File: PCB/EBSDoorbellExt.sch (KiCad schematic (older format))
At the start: 42 parts, among them P1 AC in, P2 Doorbell, Q1 BC846C, SW1 Power, SW2 Test, U1 LM7812CT, U2 LM555N

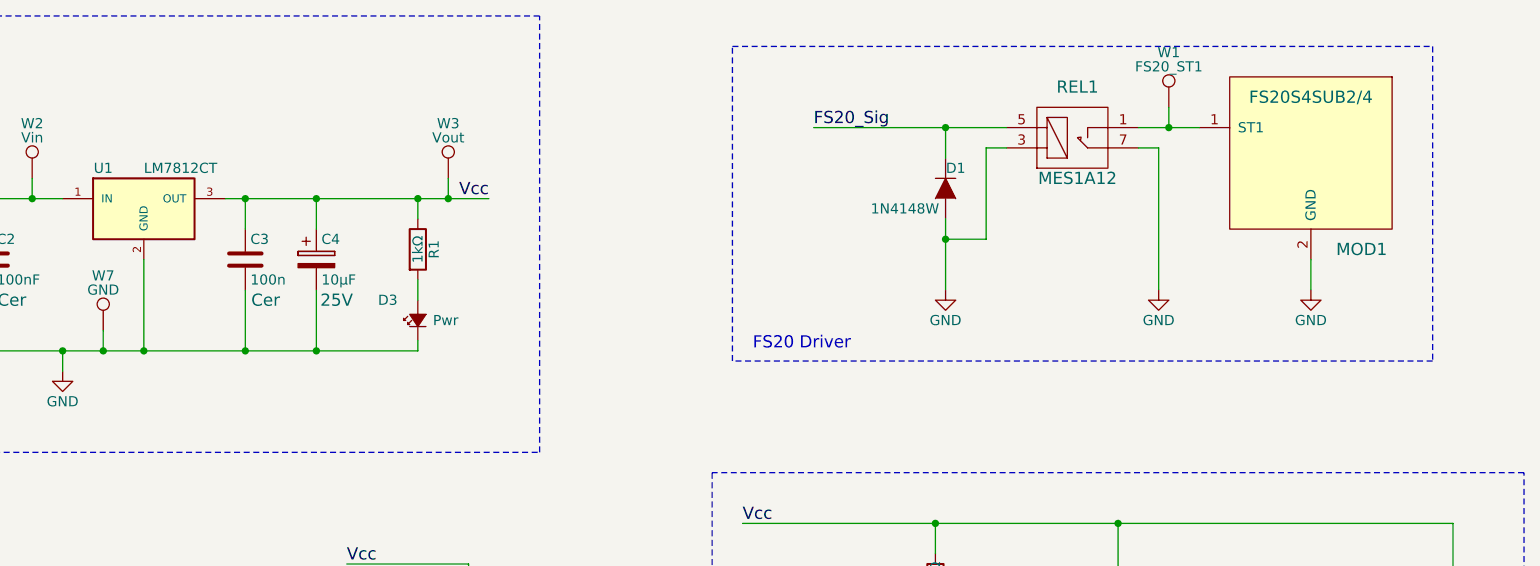
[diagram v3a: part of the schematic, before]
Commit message: Changed the layout to use an Optocoupler instead of a relay and generated Gerbers
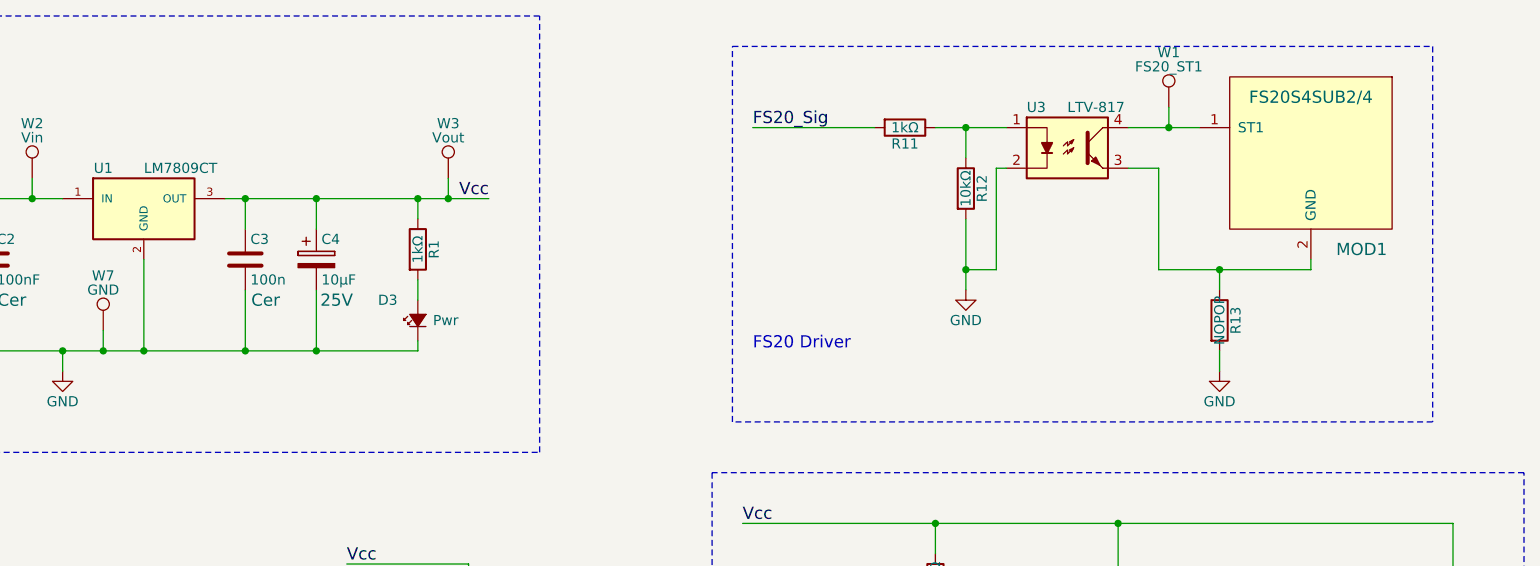
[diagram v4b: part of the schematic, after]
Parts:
- removed D1: 1N4148W, Diodes_SMD:SOD-523, symbol D
- removed REL1: MES1A12, EBSDoorbellExt-Footprints:MES1A12, symbol MES1A12
- added R11: 1kΩ, Resistors_SMD:R_0805_HandSoldering, symbol R
- added R12: 10kΩ, Resistors_SMD:R_0805_HandSoldering, symbol R
- added R13: NOPOP, Resistors_SMD:R_0805_HandSoldering, symbol R
- added U3: LTV-817, EBSDoorbellExt-Footprints:LTV_817, symbol LTV-817
- U1: value LM7812CT -> LM7809CT; footprint TO_SOT_Packages_THT:TO-220_Neutral123_Vertical -> TO_SOT_Packages_THT:TO-220_Neutral123_Horizontal; DigiKeyPN LM7812CTFS-ND -> LM7809ACT-ND
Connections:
- net FS20_Sig: now also R11.2
- net GND: now also R12.2, R13.2, U3.2; no longer MOD1.2 (GND)
- net at MOD1.1 (ST1), W1.1: now also U3.4
- new net: MOD1.2 (GND), R13.1, U3.3
- new net: R11.1, R12.1, U3.1
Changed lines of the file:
@@
 P 3750 1650
 F 0 "U1" H 3550 1850 50  0000 C CNN
-F 1 "LM7812CT" H 3750 1850 50  0000 L CNN
-F 2 "TO_SOT_Packages_THT:TO-220_Neutral123_Vertical" H 3750 1750 50  0001 C CIN
-F 3 "http://www.fairchildsemi.com/datasheets/LM/LM7805.pdf" H 3750 1650 50  0001 C CNN
-F 4 "LM7812CTFS-ND " H 3750 1650 60  0001 C CNN "DigiKeyPN"
+F 1 "LM7809CT" H 3750 1850 50  0000 L CNN
+F 2 "TO_SOT_Packages_THT:TO-220_Neutral123_Horizontal" H 3750 1750 50  0001 C CIN
+F 3 "https://www.fairchildsemi.com/datasheets/LM/LM7805.pdf" H 3750 1650 50  0001 C CNN
+F 4 "LM7809ACT-ND" H 3750 1650 60  0001 C CNN "DigiKeyPN"
 F 5 "Value" H 3750 1650 60  0001 C CNN "Voltage"
 F 6 "Value" H 3750 1650 60  0001 C CNN "ConradPN"
@@
 	5100 2350 5100 2300
 Connection ~ 4600 2350
-$Comp
-L MES1A12 REL1
-U 1 1 57543C1C
-P 8350 1300
-F 0 "REL1" H 8350 1050 60  0000 C CNN
-F 1 "MES1A12" H 8350 1500 60  0000 C CNN
-F 2 "EBSDoorbellExt-Footprints:MES1A12" H 8350 1300 60  0001 C CNN
-F 3 "" H 8350 1300 60  0000 C CNN
-F 4 "Value" H 8350 1300 60  0001 C CNN "DigiKeyPN"
-F 5 "Value" H 8350 1300 60  0001 C CNN "Voltage"
-F 6 "Value" H 8350 1300 60  0001 C CNN "ConradPN"
-F 7 "Value" H 8350 1300 60  0001 C CNN "Link"
-	1    8350 1300
-	1    0    0    1
-$EndComp
-Text Label 7050 1250 0    60   ~ 0
+Text Label 6750 1250 0    60   ~ 0
 FS20_Sig
 $Comp
 L GND #PWR05
 U 1 1 57543E6A
-P 7700 2050
-F 0 "#PWR05" H 7700 1800 50  0001 C CNN
-F 1 "GND" H 7700 1900 50  0000 C CNN
-F 2 "" H 7700 2050 50  0000 C CNN
-F 3 "" H 7700 2050 50  0000 C CNN
-	1    7700 2050
-	1    0    0    -1
-$EndComp
-Wire Wire Line
-	7050 1250 8000 1250
-Wire Wire Line
-	7700 1400 7700 1250
-Connection ~ 7700 1250
-Wire Wire Line
-	7700 1700 7700 2050
-Wire Wire Line
-	7700 1800 7900 1800
-Wire Wire Line
-	7900 1800 7900 1350
-Wire Wire Line
-	7900 1350 8000 1350
-Connection ~ 7700 1800
+P 7800 2050
+F 0 "#PWR05" H 7800 1800 50  0001 C CNN
+F 1 "GND" H 7800 1900 50  0000 C CNN
+F 2 "" H 7800 2050 50  0000 C CNN
+F 3 "" H 7800 2050 50  0000 C CNN
+	1    7800 2050
+	1    0    0    -1
+$EndComp
+Wire Wire Line
+	7650 1250 8000 1250
 $Comp
 L FS20S4SUB2/4-RESCUE-EBSDoorbellExt MOD1
@@
 $EndComp
 Wire Wire Line
-	8950 1250 8650 1250
-Wire Wire Line
-	8650 1350 8750 1350
-Wire Wire Line
-	8750 1350 8750 2050
-$Comp
-L GND #PWR06
-U 1 1 5754503D
-P 8750 2050
-F 0 "#PWR06" H 8750 1800 50  0001 C CNN
-F 1 "GND" H 8750 1900 50  0000 C CNN
-F 2 "" H 8750 2050 50  0000 C CNN
-F 3 "" H 8750 2050 50  0000 C CNN
-	1    8750 2050
-	1    0    0    -1
-$EndComp
-Wire Wire Line
-	9500 1900 9500 2050
-$Comp
-L GND #PWR07
-U 1 1 575450F0
-P 9500 2050
-F 0 "#PWR07" H 9500 1800 50  0001 C CNN
-F 1 "GND" H 9500 1900 50  0000 C CNN
-F 2 "" H 9500 2050 50  0000 C CNN
-F 3 "" H 9500 2050 50  0000 C CNN
-	1    9500 2050
-	1    0    0    -1
-$EndComp
+	8600 1250 8950 1250
 Wire Wire Line
 	2150 2200 2150 2000
@@
 Connection ~ 3550 4250
 $Comp
-L GND #PWR08
+L GND #PWR06
 U 1 1 57548DD0
 P 2450 5200
-F 0 "#PWR08" H 2450 4950 50  0001 C CNN
+F 0 "#PWR06" H 2450 4950 50  0001 C CNN
 F 1 "GND" H 2450 5050 50  0000 C CNN
 F 2 "" H 2450 5200 50  0000 C CNN
@@
 	2450 5200 2450 5050
 $Comp
-L GND #PWR09
+L GND #PWR07
 U 1 1 57548ECC
 P 3250 5200
-F 0 "#PWR09" H 3250 4950 50  0001 C CNN
+F 0 "#PWR07" H 3250 4950 50  0001 C CNN
 F 1 "GND" H 3250 5050 50  0000 C CNN
 F 2 "" H 3250 5200 50  0000 C CNN
@@
 	3250 5200 3250 4900
 $Comp
-L GND #PWR010
+L GND #PWR08
 U 1 1 5754905C
 P 3550 5200
-F 0 "#PWR010" H 3550 4950 50  0001 C CNN
+F 0 "#PWR08" H 3550 4950 50  0001 C CNN
 F 1 "GND" H 3550 5050 50  0000 C CNN
 F 2 "" H 3550 5200 50  0000 C CNN
@@
 Connection ~ 4850 4250
 $Comp
-L GND #PWR011
+L GND #PWR09
 U 1 1 5754947D
 P 4550 5200
-F 0 "#PWR011" H 4550 4950 50  0001 C CNN
+F 0 "#PWR09" H 4550 4950 50  0001 C CNN
 F 1 "GND" H 4550 5050 50  0000 C CNN
 F 2 "" H 4550 5200 50  0000 C CNN
@@
 $EndComp
 $Comp
-L GND #PWR012
+L GND #PWR010
 U 1 1 57549484
 P 4850 5200
-F 0 "#PWR012" H 4850 4950 50  0001 C CNN
+F 0 "#PWR010" H 4850 4950 50  0001 C CNN
 F 1 "GND" H 4850 5050 50  0000 C CNN
 F 2 "" H 4850 5200 50  0000 C CNN
@@
 	4550 4900 4550 5200
 $Comp
-L GND #PWR013
+L GND #PWR011
 U 1 1 57549A88
 P 1800 5200
-F 0 "#PWR013" H 1800 4950 50  0001 C CNN
+F 0 "#PWR011" H 1800 4950 50  0001 C CNN
 F 1 "GND" H 1800 5050 50  0000 C CNN
 F 2 "" H 1800 5200 50  0000 C CNN
@@
 ~Trigger
 $Comp
-L GND #PWR014
+L GND #PWR012
 U 1 1 5754A014
 P 5350 5200
-F 0 "#PWR014" H 5350 4950 50  0001 C CNN
+F 0 "#PWR012" H 5350 4950 50  0001 C CNN
 F 1 "GND" H 5350 5050 50  0000 C CNN
 F 2 "" H 5350 5200 50  0000 C CNN
@@
 Wire Wire Line
 	2150 900  2150 1200
-$Comp
-L D D1
-U 1 1 5754BDF2
-P 7700 1550
-F 0 "D1" V 7600 1600 50  0000 C CNN
-F 1 "1N4148W" V 7800 1350 50  0000 C CNN
-F 2 "Diodes_SMD:SOD-523" H 7700 1550 50  0001 C CNN
-F 3 "http://www.vishay.com/docs/85887/1n4148wfl-g.pdf" H 7700 1550 50  0001 C CNN
-F 4 "1N4148WFL-G3-08GICT-ND" H 7700 1550 60  0001 C CNN "DigiKeyPN"
-F 5 "Value" H 7700 1550 60  0001 C CNN "Voltage"
-F 6 "Value" H 7700 1550 60  0001 C CNN "ConradPN"
-F 7 "Value" H 7700 1550 60  0001 C CNN "Link"
-	1    7700 1550
-	0    1    1    0
-$EndComp
-Wire Notes Line
-	10100 850  10100 2400
-Wire Notes Line
-	10100 2400 6650 2400
-Wire Notes Line
-	6650 2400 6650 850
 Wire Notes Line
 	600  700  600  2850
@@
 	3550 2250 3550 2350
 Connection ~ 3550 2350
+$Comp
+L GND #PWR013
+U 1 1 57583E08
+P 9050 2450
+F 0 "#PWR013" H 9050 2200 50  0001 C CNN
+F 1 "GND" H 9050 2300 50  0000 C CNN
+F 2 "" H 9050 2450 50  0000 C CNN
+F 3 "" H 9050 2450 50  0000 C CNN
+	1    9050 2450
+	1    0    0    -1
+$EndComp
+$Comp
+L R R12
+U 1 1 57584654
+P 7800 1550
+F 0 "R12" V 7880 1550 50  0000 C CNN
+F 1 "10kΩ" V 7800 1550 50  0000 C CNN
+F 2 "Resistors_SMD:R_0805_HandSoldering" V 7730 1550 50  0001 C CNN
+F 3 "" H 7800 1550 50  0000 C CNN
+	1    7800 1550
+	1    0    0    -1
+$EndComp
+Wire Notes Line
+	10100 2700 6650 2700
+$Comp
+L LTV-817 U3
+U 1 1 575EDEE6
+P 8300 1350
+F 0 "U3" H 8100 1550 50  0000 L CNN
+F 1 "LTV-817" H 8300 1550 50  0000 L CNN
+F 2 "EBSDoorbellExt-Footprints:LTV_817" H 8100 1150 50  0001 L CIN
+F 3 "http://optoelectronics.liteon.com/upload/download/DS70-2012-0050/S_110_LTV-817%20%28M,%20S,%20S-TA,%20S-TA1,%20S-TP%29%20Series%2020130925.pdf" H 8300 1250 50  0001 L CNN
+F 4 "160-1367-5-ND " H 8300 1350 60  0001 C CNN "DigiKeyPN"
+F 5 "Value" H 8300 1350 60  0001 C CNN "Voltage"
+F 6 "Value" H 8300 1350 60  0001 C CNN "ConradPN"
+F 7 "Value" H 8300 1350 60  0001 C CNN "Link"
+	1    8300 1350
+	1    0    0    -1
+$EndComp
+Wire Wire Line
+	7800 1250 7800 1400
+Wire Wire Line
+	7800 1700 7800 2050
+Wire Wire Line
+	8000 1450 7950 1450
+Wire Wire Line
+	7950 1450 7950 1950
+Wire Wire Line
+	7950 1950 7800 1950
+Connection ~ 7800 1950
+Wire Notes Line
+	10100 850  10100 2700
+Wire Notes Line
+	6650 2700 6650 850
+$Comp
+L R R13
+U 1 1 575EF20B
+P 9050 2200
+F 0 "R13" V 9130 2200 50  0000 C CNN
+F 1 "NOPOP" V 9050 2200 50  0000 C CNN
+F 2 "Resistors_SMD:R_0805_HandSoldering" V 8980 2200 50  0001 C CNN
+F 3 "" H 9050 2200 50  0000 C CNN
+F 4 "Value" H 9050 2200 60  0001 C CNN "DigiKeyPN"
+F 5 "Value" H 9050 2200 60  0001 C CNN "Voltage"
+F 6 "Value" H 9050 2200 60  0001 C CNN "ConradPN"
+F 7 "Value" H 9050 2200 60  0001 C CNN "Link"
+	1    9050 2200
+	1    0    0    -1
+$EndComp
+Wire Wire Line
+	8600 1450 8750 1450
+Wire Wire Line
+	8750 1450 8750 1950
+Wire Wire Line
+	8750 1950 9500 1950
+Wire Wire Line
+	9500 1950 9500 1900
+Wire Wire Line
+	9050 1950 9050 2050
+Connection ~ 9050 1950
+Wire Wire Line
+	9050 2350 9050 2450
+$Comp
+L R R11
+U 1 1 575EFDA3
+P 7500 1250
+F 0 "R11" V 7580 1250 50  0000 C CNN
+F 1 "1kΩ" V 7500 1250 50  0000 C CNN
+F 2 "Resistors_SMD:R_0805_HandSoldering" V 7430 1250 50  0001 C CNN
+F 3 "" H 7500 1250 50  0000 C CNN
+	1    7500 1250
+	0    1    1    0
+$EndComp
+Wire Wire Line
+	6750 1250 7350 1250
+Connection ~ 7800 1250
 $EndSCHEMATC

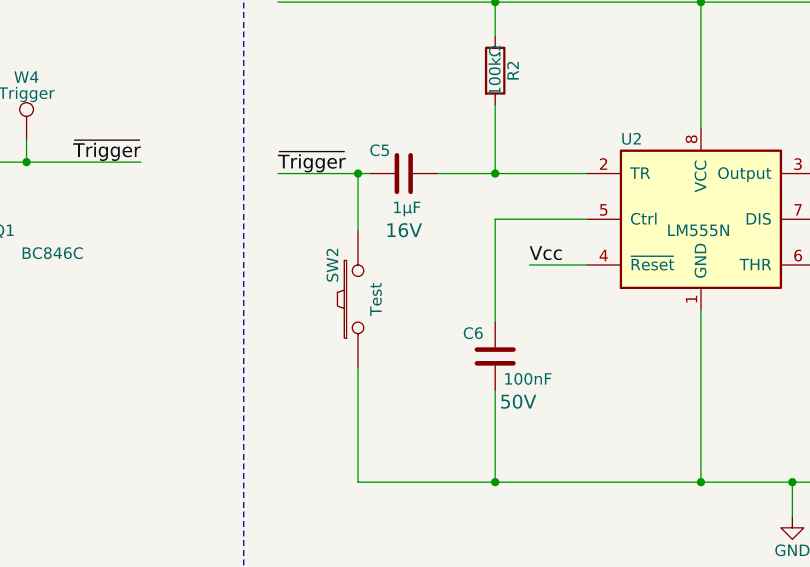
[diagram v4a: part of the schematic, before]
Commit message: Corrected some footprint issues
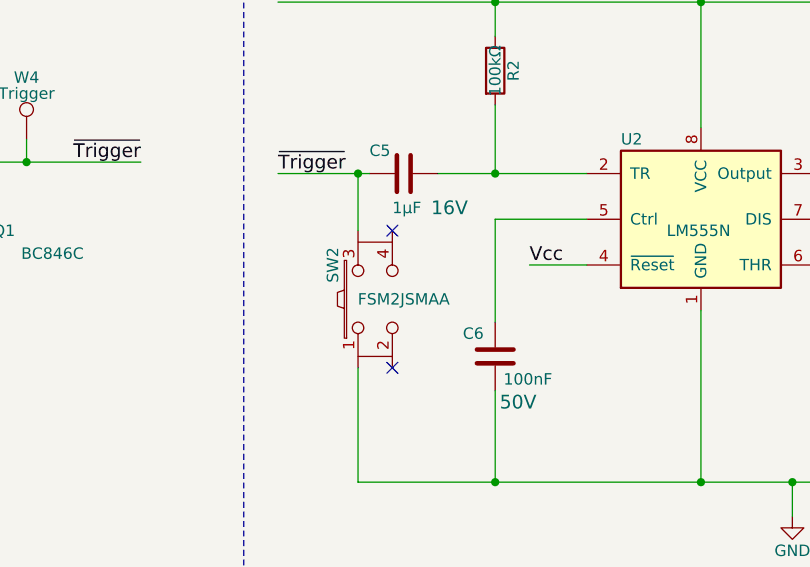
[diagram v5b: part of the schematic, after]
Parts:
- removed SW2: Test, EBSDoorbellExt-Footprints:FSM2JSMAA, symbol SW_PUSH
- added SW2: FSM2JSMAA, EBSDoorbellExt-Footprints:FSM2JSMAA, symbol FSM2JSMAA
- D4: footprint Diodes_SMD:SOD-523 -> Diodes_SMD:SOD-123
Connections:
- net GND: now also SW2.1
- net ~Trigger: now also SW2.3
- no-connect marks 0 -> 2

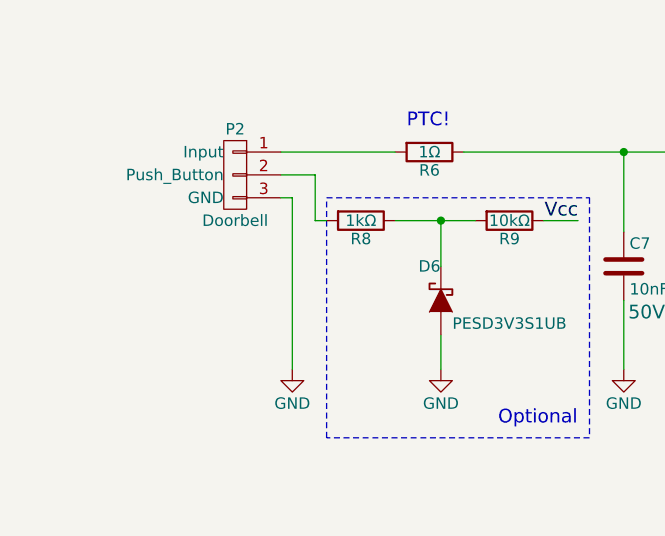
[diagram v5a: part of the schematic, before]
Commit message: Added protection diode on ground for voltage sensing
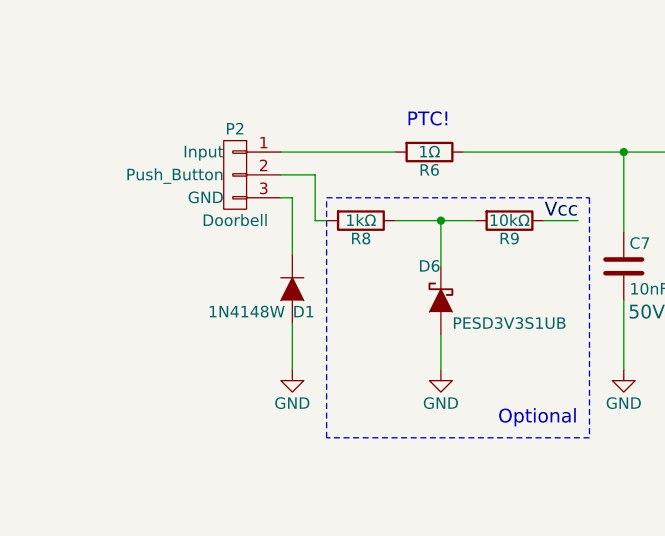
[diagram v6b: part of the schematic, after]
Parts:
- added D1: 1N4148W, Diodes_SMD:SOD-123, symbol D
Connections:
- net GND: now also D1.2 (A); no longer P2.3 (GND)
- new net: D1.1 (K), P2.3 (GND)
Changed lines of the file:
@@
 FS20_Sig
 $Comp
-L GND #PWR13
+L GND #PWR01
 U 1 1 5753FA0F
 P 8950 5450
-F 0 "#PWR13" H 8950 5200 50  0001 C CNN
+F 0 "#PWR01" H 8950 5200 50  0001 C CNN
 F 1 "GND" H 8950 5300 50  0000 C CNN
 F 2 "" H 8950 5450 50  0000 C CNN
@@
 $EndComp
 $Comp
-L GND #PWR5
+L GND #PWR02
 U 1 1 575401BA
 P 9450 4650
-F 0 "#PWR5" H 9450 4400 50  0001 C CNN
+F 0 "#PWR02" H 9450 4400 50  0001 C CNN
 F 1 "GND" H 9450 4500 50  0000 C CNN
 F 2 "" H 9450 4650 50  0000 C CNN
@@
 $EndComp
 $Comp
-L GND #PWR3
+L GND #PWR03
 U 1 1 575417A1
 P 3350 2450
-F 0 "#PWR3" H 3350 2200 50  0001 C CNN
+F 0 "#PWR03" H 3350 2200 50  0001 C CNN
 F 1 "GND" H 3350 2300 50  0000 C CNN
 F 2 "" H 3350 2450 50  0000 C CNN
@@
 $EndComp
 $Comp
-L GND #PWR1
+L GND #PWR04
 U 1 1 57541A3A
 P 1750 1800
-F 0 "#PWR1" H 1750 1550 50  0001 C CNN
+F 0 "#PWR04" H 1750 1550 50  0001 C CNN
 F 1 "GND" H 1750 1650 50  0000 C CNN
 F 2 "" H 1750 1800 50  0000 C CNN
@@
 FS20_Sig
 $Comp
-L GND #PWR2
+L GND #PWR05
 U 1 1 57543E6A
 P 7800 2050
-F 0 "#PWR2" H 7800 1800 50  0001 C CNN
+F 0 "#PWR05" H 7800 1800 50  0001 C CNN
 F 1 "GND" H 7800 1900 50  0000 C CNN
 F 2 "" H 7800 2050 50  0000 C CNN
@@
 Connection ~ 3550 4250
 $Comp
-L GND #PWR7
+L GND #PWR06
 U 1 1 57548DD0
 P 2450 5200
-F 0 "#PWR7" H 2450 4950 50  0001 C CNN
+F 0 "#PWR06" H 2450 4950 50  0001 C CNN
 F 1 "GND" H 2450 5050 50  0000 C CNN
 F 2 "" H 2450 5200 50  0000 C CNN
@@
 	2450 5200 2450 5050
 $Comp
-L GND #PWR8
+L GND #PWR07
 U 1 1 57548ECC
 P 3250 5200
-F 0 "#PWR8" H 3250 4950 50  0001 C CNN
+F 0 "#PWR07" H 3250 4950 50  0001 C CNN
 F 1 "GND" H 3250 5050 50  0000 C CNN
 F 2 "" H 3250 5200 50  0000 C CNN
@@
 	3250 5200 3250 4900
 $Comp
-L GND #PWR9
+L GND #PWR08
 U 1 1 5754905C
 P 3550 5200
-F 0 "#PWR9" H 3550 4950 50  0001 C CNN
+F 0 "#PWR08" H 3550 4950 50  0001 C CNN
 F 1 "GND" H 3550 5050 50  0000 C CNN
 F 2 "" H 3550 5200 50  0000 C CNN
@@
 Connection ~ 4850 4250
 $Comp
-L GND #PWR10
+L GND #PWR09
 U 1 1 5754947D
 P 4550 5200
-F 0 "#PWR10" H 4550 4950 50  0001 C CNN
+F 0 "#PWR09" H 4550 4950 50  0001 C CNN
 F 1 "GND" H 4550 5050 50  0000 C CNN
 F 2 "" H 4550 5200 50  0000 C CNN
@@
 $EndComp
 $Comp
-L GND #PWR11
+L GND #PWR010
 U 1 1 57549484
 P 4850 5200
-F 0 "#PWR11" H 4850 4950 50  0001 C CNN
+F 0 "#PWR010" H 4850 4950 50  0001 C CNN
 F 1 "GND" H 4850 5050 50  0000 C CNN
 F 2 "" H 4850 5200 50  0000 C CNN
@@
 	4550 4900 4550 5200
 $Comp
-L GND #PWR6
+L GND #PWR011
 U 1 1 57549A88
 P 1800 5200
-F 0 "#PWR6" H 1800 4950 50  0001 C CNN
+F 0 "#PWR011" H 1800 4950 50  0001 C CNN
 F 1 "GND" H 1800 5050 50  0000 C CNN
 F 2 "" H 1800 5200 50  0000 C CNN
@@
 	1    0    0    -1
 $EndComp
-Wire Wire Line
-	1750 4450 1800 4450
-Wire Wire Line
-	1800 4450 1800 5200
 Text Label 6100 3900 2    60   ~ 0
 ~Trigger
 $Comp
-L GND #PWR12
+L GND #PWR012
 U 1 1 5754A014
 P 5350 5200
-F 0 "#PWR12" H 5350 4950 50  0001 C CNN
+F 0 "#PWR012" H 5350 4950 50  0001 C CNN
 F 1 "GND" H 5350 5050 50  0000 C CNN
 F 2 "" H 5350 5200 50  0000 C CNN
@@
 Connection ~ 3550 2350
 $Comp
-L GND #PWR4
+L GND #PWR013
 U 1 1 57583E08
 P 9050 2450
-F 0 "#PWR4" H 9050 2200 50  0001 C CNN
+F 0 "#PWR013" H 9050 2200 50  0001 C CNN
 F 1 "GND" H 9050 2300 50  0000 C CNN
 F 2 "" H 9050 2450 50  0000 C CNN
@@
 NoConn ~ 7200 4200
 NoConn ~ 7200 4800
+$Comp
+L D D1
+U 1 1 57717B4C
+P 1800 4850
+F 0 "D1" V 1900 4900 50  0000 C CNN
+F 1 "1N4148W" V 1900 4650 50  0000 C CNN
+F 2 "Diodes_SMD:SOD-123" H 1800 4850 50  0001 C CNN
+F 3 "http://www.vishay.com/docs/85887/1n4148wfl-g.pdf" H 1800 4850 50  0001 C CNN
+F 4 "1N4148WFL-G3-08GICT-ND" H 1800 4850 60  0001 C CNN "DigiKeyPN"
+F 5 "Value" H 1800 4850 60  0001 C CNN "Voltage"
+F 6 "Value" H 1800 4850 60  0001 C CNN "ConradPN"
+F 7 "Value" H 1800 4850 60  0001 C CNN "Link"
+	1    1800 4850
+	0    1    1    0
+$EndComp
+Wire Wire Line
+	1750 4450 1800 4450
+Wire Wire Line
+	1800 4450 1800 4700
+Wire Wire Line
+	1800 5000 1800 5200
 $EndSCHEMATC
